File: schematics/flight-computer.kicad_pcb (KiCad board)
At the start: 4 copper layers, 80 x 80 mm, 59 parts, among them J1 BATT, J2 BLACKBOX, J3 BMI-S-201, P1 GPS, P2 TLM, U1 STM32F405RGT6, U2 MAX14787E, U4 MS5611-01BA, U6 Si4463, U7 MAX-M8Q, U8 MAX604, U9 MAX604

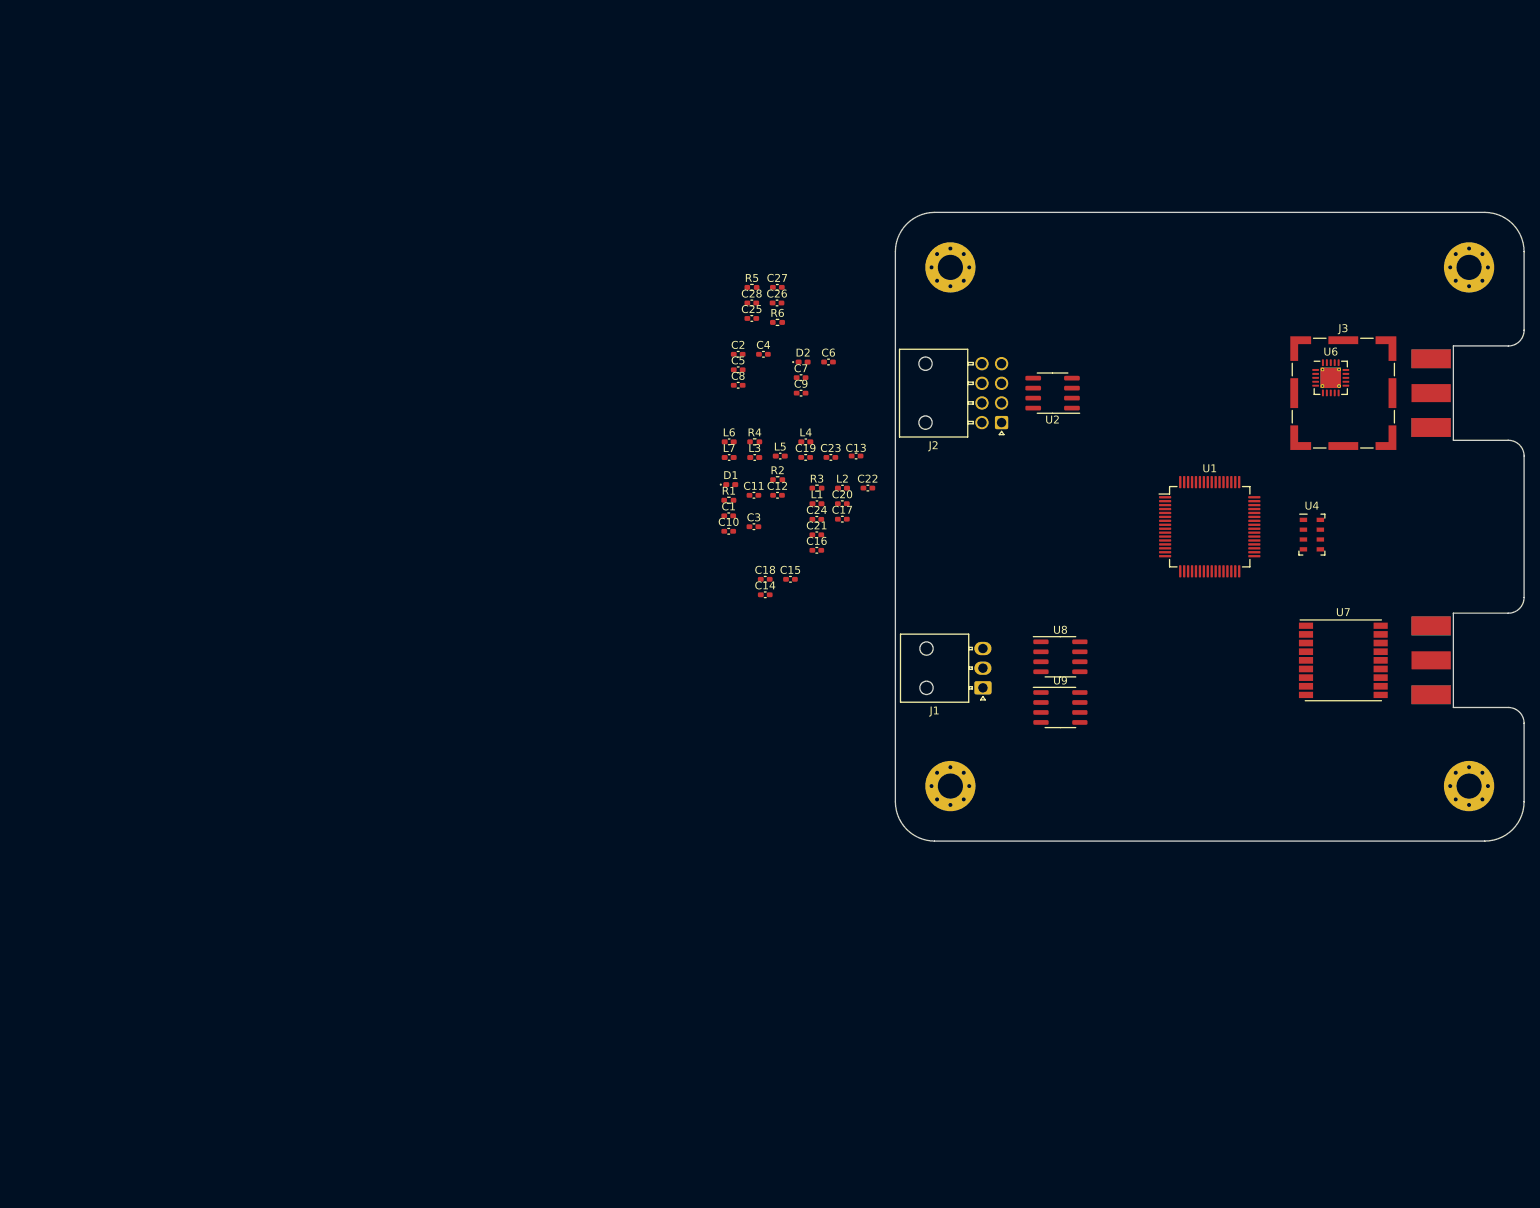
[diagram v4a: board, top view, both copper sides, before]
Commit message: Add missing IC footprints
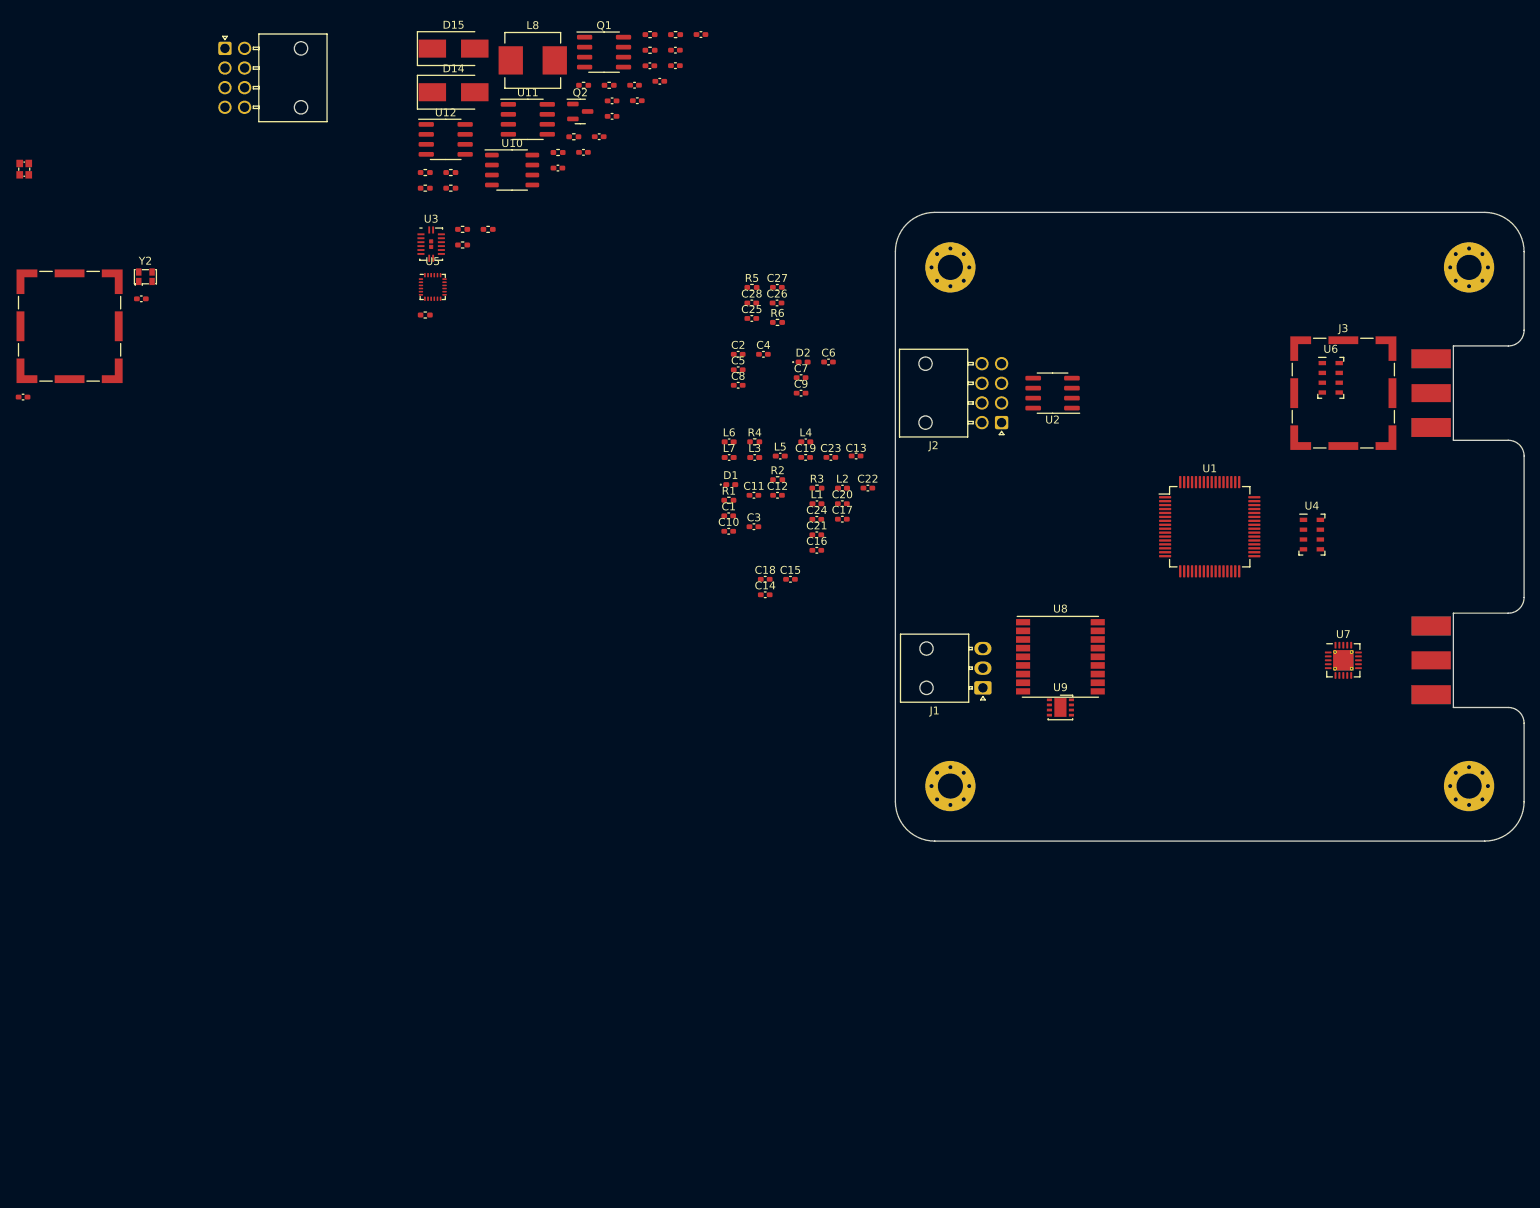
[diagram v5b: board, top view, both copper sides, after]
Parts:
- removed P1: GPS, Strix:SMA-EDGE
- removed P2: TLM, Strix:SMA-EDGE
- added C29: 3p3, Strix:C_0402, F.Cu at (144.0, 118.5)
- added C30: 3p3, Strix:C_0402, F.Cu at (159.1, 106.0)
- added C31: 100n, Strix:C_0402, F.Cu at (218.9, 82.8)
- added C32: 100n, Strix:C_0402, F.Cu at (222.2, 80.8)
- added C33: 330n, Strix:C_0402, F.Cu at (215.3, 87.4)
- added C34: 100n, Strix:C_0402, F.Cu at (221.8, 78.8)
- added C35: 470n, Strix:C_0402, F.Cu at (230.3, 72.4)
- added C36: 10u, Strix:C_0402, F.Cu at (223.8, 76.3)
- added C37: 100n, Strix:C_0402, F.Cu at (227.0, 76.3)
- added C38: 22u, Strix:C_0402, F.Cu at (227.0, 74.4)
- added C39: 10u, Strix:C_0402, F.Cu at (212.1, 89.4)
- added C40: 10u, Strix:C_0402, F.Cu at (218.9, 80.8)
- added C41: 10u, Strix:C_0402, F.Cu at (225.0, 78.3)
- added C42: 10u, Strix:C_0402, F.Cu at (217.3, 85.4)
- added D14: B330, Strix:B330, F.Cu at (198.8, 79.7)
- added D15: B330, Strix:B330, F.Cu at (198.8, 74.2)
- added J4: GPS, Strix:SMA-Edge, F.Cu at (323.2, 152.0)
- added J5: TELEM, Strix:SMA-Edge, F.Cu at (323.2, 118.0)
- added J7: BLACKBOX, Strix:Molex_Nano-Fit_105314-1108, F.Cu at (169.7, 74.1)
- added J8: BMI-S-201, Strix:BMI-S-201, F.Cu at (149.9, 109.5)
- added L8: 6u8, Strix:L_Wuerth_HCI-7050, F.Cu at (208.9, 75.7)
- added Q1: Si9933CDY, Strix:Si9933CDY, F.Cu at (217.9, 74.6)
- added Q2: BSS138, Strix:BSS138, F.Cu at (214.9, 82.2)
- added R10: 4k7, Strix:R_0402, F.Cu at (199.9, 97.2)
- added R11: 100k, Strix:R_0402, F.Cu at (212.1, 87.4)
- added R12: 160, Strix:R_0402, F.Cu at (214.1, 85.4)
- added R13: 261, Strix:R_0402, F.Cu at (223.8, 72.4)
- added R14: 100, Strix:R_0402, F.Cu at (218.6, 78.8)
- added R15: 10k, Strix:R_0402, F.Cu at (215.3, 78.8)
- added R16: 100, Strix:R_0402, F.Cu at (195.2, 89.9)
- added R17: 100, Strix:R_0402, F.Cu at (227.0, 72.4)
- added R18: 2k2, Strix:R_0402, F.Cu at (198.4, 89.9)
- added R19: 50m, Strix:R_0402, F.Cu at (223.8, 74.4)
- added R20: 200k, Strix:R_0402, F.Cu at (195.2, 91.9)
- added R21: 100k, Strix:R_0402, F.Cu at (198.4, 91.9)
- added R7: 4k7, Strix:R_0402, F.Cu at (203.2, 97.2)
- added R8: 200k, Strix:R_0402, F.Cu at (199.9, 99.2)
- added R9: 4k7, Strix:R_0402, F.Cu at (195.2, 108.1)
- added U10: LTC4002-ES8, Strix:LTC4002-ES8, F.Cu at (206.2, 89.6)
- added U11: MAX604, Strix:MAX604, F.Cu at (208.2, 83.2)
- added U12: MAX604, Strix:MAX604, F.Cu at (197.8, 85.7)
- added U3: NVT2006BQ, Strix:NVT2006BQ, F.Cu at (195.9, 99.0)
- added U5: ICM-20789, Strix:ICM-20789, F.Cu at (196.1, 104.5)
- added Y1: 26M, Strix:Xtal-20x16, F.Cu at (144.2, 89.5)
- added Y2: LFTCXO068373, Strix:LFTCXO068373, F.Cu at (159.6, 103.2)
- C1: value 1µ -> 10p
- C10, C11: value 100n -> 2µ2
- C13: value 100n -> 100p
- C14: value 1u -> 15p
- C15: value 2u2 -> 100p
- C16: value 100n -> 15p
- C17: value 220p -> 100n
- C18: value 100p -> 2n
- C19: value 3p -> 100n
- C2: value 4µ7 -> 10p
- C20: value 5p1 -> 1u
- C21: value 1p2 -> 2u2
- C22: value 6n8 -> 100n
- C23: value 3p3 -> 220p
- C24: value 3p3 -> 100p
- C25: value 10u -> 3p
- C26: value 10u -> 5p1
- C27: value 10u -> 1p2
- C28: value 10u -> 6n8
- C3: value 100n -> 1µ
- C4: value 100n -> 4µ7
- C8, C9: value 2µ2 -> 100n
- R1: value 120 -> 100
- R2: value 100k -> 10k
- R4: value 10k -> 120
- R5: value 200k -> 4k7
- R6: value 100k -> 200k
- U6: value Si4463 -> MS5611-01BA; footprint Strix:Si4463 -> Strix:MS5611-01BA
- U7: value MAX-M8Q -> Si4463; footprint Strix:MAX-M8Q -> Strix:Si4463
- U8: value MAX604 -> MAX-M8Q; footprint Strix:MAX604 -> Strix:MAX-M8Q
- U9: value MAX604 -> BQ29200; footprint Strix:MAX604 -> Strix:BQ29200
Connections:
- net /Radio/RADIO_CLK renamed Net-(D5-Pad2)
- C1 pad 2: 3v3 -> Net-(C1-Pad2)
- C10 pad 2: /~{RST} -> Net-(C10-Pad2)
- C11 pad 1: 3v3 -> GND
- C11 pad 2: GND -> Net-(C11-Pad2)
- C12 pad 1: 1v8 -> GND
- C12 pad 2: unconnected-(C12-Pad2) -> /NRST
- C14 pad 1: 3v3 -> GND
- C14 pad 2: GND -> Net-(C14-Pad2)
- C15 pad 1: 3v3 -> GND
- C15 pad 2: GND -> 3v3
- C16 pad 1: 3v3 -> GND
- C16 pad 2: GND -> Net-(C16-Pad2)
- C17 pad 1: 3v3 -> 1v8
- C18 pad 1: 3v3 -> Net-(C18-Pad1)
- C18 pad 2: GND -> Net-(C18-Pad2)
- C19 pad 1: /Radio/RX+ -> GND
- C19 pad 2: GND -> 3v3
- C2 pad 2: 3v3 -> Net-(C2-Pad2)
- C20 pad 1: /Radio/TX -> 3v3
- C20 pad 2: Net-(C20-Pad2) -> GND
- C21 pad 1: /Radio/RX- -> 3v3
- C21 pad 2: Net-(C21-Pad2) -> GND
- C22 pad 1: Net-(C21-Pad2) -> 3v3
- C23 pad 1: Net-(C23-Pad1) -> 3v3
- C24 pad 1: Net-(C24-Pad1) -> 3v3
- C25 pad 1: VBATT -> /Radio/RX+
- C26 pad 1: VBATT -> /Radio/TX
- C26 pad 2: GND -> Net-(C26-Pad2)
- C27 pad 1: 3v3 -> /Radio/RX-
- C27 pad 2: GND -> Net-(C27-Pad2)
- C28 pad 1: 1v8 -> Net-(C27-Pad2)
- C8 pad 2: Net-(C8-Pad2) -> 3v3
- C9 pad 2: Net-(C9-Pad2) -> 3v3
- J1 pad 1: /PSU/BATT+ -> VBATT
- J1 pad 3: /PSU/BATT- -> GND
- L3 pad 1: Net-(C20-Pad2) -> Net-(C26-Pad2)
- L3 pad 2: Net-(C21-Pad2) -> Net-(C27-Pad2)
- L4 pad 2: Net-(C21-Pad2) -> Net-(C27-Pad2)
- L5 pad 1: Net-(C21-Pad2) -> Net-(C27-Pad2)
- L5 pad 2: Net-(C23-Pad1) -> Net-(C29-Pad1)
- L6 pad 1: Net-(C23-Pad1) -> Net-(C29-Pad1)
- L6 pad 2: Net-(C24-Pad1) -> Net-(C30-Pad1)
- L7 pad 1: Net-(C24-Pad1) -> Net-(C30-Pad1)
- R1 pad 1: /UART4_RX+ -> Net-(C2-Pad2)
- R1 pad 2: /UART4_RX- -> Net-(R1-Pad2)
- R2 pad 1: 1v8 -> GND
- R2 pad 2: GND -> /USB_FS_VBUS
- R3 pad 1: /Radio/RADIO_CLK_1.65V -> /USB_FS_VBUS
- R4 pad 1: /Radio/RADIO_CLK_1.65V -> /BB_RX+
- R4 pad 2: GND -> /BB_RX-
- R5 pad 1: Net-(R5-Pad1) -> 3v3
- R5 pad 2: GND -> /IMU_PR_CL
- R6 pad 1: Net-(R5-Pad1) -> 3v3
- R6 pad 2: 1v8 -> Net-(C14-Pad2)
- U1 pad 31: Net-(C8-Pad2) -> Net-(C10-Pad2)
- U1 pad 42: unconnected-(U1-Pad42) -> /USB_FS_VBUS
- U1 pad 44: unconnected-(U1-Pad44) -> /USB_FS_D+
- U1 pad 45: unconnected-(U1-Pad45) -> /USB_FS_D-
- U1 pad 47: Net-(C9-Pad2) -> Net-(C11-Pad2)
- U1 pad 5: /MCU_CLK -> Net-(C1-Pad2)
- U1 pad 50: unconnected-(U1-Pad50) -> /CHG_SDN
- U1 pad 58: unconnected-(U1-Pad58) -> /IMU_PR_CL
- U1 pad 59: unconnected-(U1-Pad59) -> /IMU_PR_DA
- U1 pad 6: unconnected-(U1-Pad6) -> Net-(R1-Pad2)
- U1 pad 7: /~{RST} -> /NRST
- U2 pad 5: /UART4_TX+ -> /BB_TX+
- U2 pad 6: /UART4_TX- -> /BB_TX-
- U2 pad 7: /UART4_RX- -> /BB_RX-
- U2 pad 8: /UART4_RX+ -> /BB_RX+
- U6 pad 1: /RADIO_SDN -> 3v3
- U6 pad 2: /Radio/RX+ -> GND
- U6 pad 3: /Radio/RX- -> GND
- U6 pad 4: /Radio/TX -> /BARO_~{CS}
- U6 pad 5: unconnected-(U6-Pad5) -> /BARO_~{CS}
- U6 pad 6: 3v3 -> /SPI3_MISO
- U6 pad 7: unconnected-(U6-Pad7) -> /SPI3_MOSI
- U6 pad 8: 3v3 -> /SPI3_SCLK
- U7 pad 1: GND -> /RADIO_SDN
- U7 pad 10: GND -> unconnected-(U7-Pad10)
- U7 pad 11: /Radio/ANT_GPS -> /RADIO_~{INT}
- U7 pad 12: GND -> /SPI2_SCLK
- U7 pad 13: unconnected-(U7-Pad13) -> /SPI2_MISO
- U7 pad 14: unconnected-(U7-Pad14) -> /SPI2_MOSI
- U7 pad 15: unconnected-(U7-Pad15) -> /RADIO_~{CS}
- U7 pad 17: unconnected-(U7-Pad17) -> Net-(C18-Pad2)
- U7 pad 18: unconnected-(U7-Pad18) -> GND
- U7 pad 2: /USART3_RX -> /Radio/RX+
- U7 pad 3: /USART3_TX -> /Radio/RX-
- U7 pad 4: unconnected-(U7-Pad4) -> /Radio/TX
- U7 pad 7: 3v3 -> unconnected-(U7-Pad7)
- U7 pad 9: /GPS_~{RESET} -> unconnected-(U7-Pad9)
- U8 pad 1: VBATT -> GND
- U8 pad 2: GND -> /USART3_RX
- U8 pad 3: GND -> /USART3_TX
- U8 pad 4: VBATT -> unconnected-(U8-Pad4)
- U8 pad 5: GND -> unconnected-(U8-Pad5)
- U8 pad 6: GND -> 3v3
- U8 pad 7: GND -> 3v3
- U9 pad 1: VBATT -> Net-(C31-Pad1)
- U9 pad 2: GND -> Net-(C31-Pad2)
- U9 pad 3: GND -> Net-(R14-Pad2)
- U9 pad 4: VBATT -> Net-(C33-Pad1)
- U9 pad 5: Net-(R5-Pad1) -> GND
- U9 pad 7: GND -> Net-(C37-Pad1)
- U9 pad 8: 1v8 -> unconnected-(U9-Pad8)

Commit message: Fix outdated footprint references in symbol lib
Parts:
- removed J2: BLACKBOX, Strix:Molex_Nano-Fit_105314-1108
- removed J3: BMI-S-201, Strix:BMI-S-201
- added D10: D_ESD, Strix:D_0402, F.Cu at (167.6, 121.0)
- added D11: D_ESD, Strix:D_0402, F.Cu at (154.0, 123.6)
- added D12: D_ESD, Strix:D_0402, F.Cu at (168.0, 123.0)
- added D13: D_ESD, Strix:D_0402, F.Cu at (187.8, 100.1)
- added D3: D_ESD, Strix:D_0402, F.Cu at (164.5, 123.6)
- added D4: D_ESD, Strix:D_0402, F.Cu at (161.0, 123.6)
- added D5: D_ESD, Strix:D_0402, F.Cu at (187.8, 104.1)
- added D6: D_ESD, Strix:D_0402, F.Cu at (176.0, 114.6)
- added D7: D_ESD, Strix:D_0402, F.Cu at (157.5, 123.6)
- added D8: D_ESD, Strix:D_0402, F.Cu at (187.8, 102.1)
- added D9: D_ESD, Strix:D_0402, F.Cu at (184.3, 106.0)
- D1, D2: value ESD_DIODE -> D_ESD
- U4: value MS5611-01BA -> PCA9306; footprint Strix:MS5611-01BA -> Strix:PCA9306
- moved U1 123.2 mm to (175.2, 106.4)
- moved U9 121.6 mm to (154.8, 147.7)
- moved J1 119.0 mm to (154.3, 114.9), turned to 0 degrees
- moved U6 115.4 mm to (197.0, 137.6)
- moved U4 109.2 mm to (198.9, 131.1)
- moved U2 105.1 mm to (169.9, 116.8), turned to 0 degrees
- moved U7 100.5 mm to (219.0, 113.9)
- moved R13 90.6 mm to (170.7, 145.8)
- moved R19 84.6 mm to (172.7, 141.8)
- moved C37 83.9 mm to (177.1, 143.8)
- moved C40 82.6 mm to (170.7, 147.8)
- moved R17 82.3 mm to (173.9, 135.3)
- moved C32 80.9 mm to (173.9, 145.8)
- moved C34 80.7 mm to (173.9, 143.8)
- moved C35 77.9 mm to (183.7, 134.8)
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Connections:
- D1 pad 1: /Radio/ANT_GPS -> /PSU/BATT_MON
- D2 pad 1: /Radio/ANT_TLM -> /PSU/CHG+
- U4 pad 1: 3v3 -> GND
- U4 pad 2: GND -> 1v8
- U4 pad 3: GND -> Net-(R9-Pad2)
- U4 pad 4: /BARO_~{CS} -> Net-(R10-Pad2)
- U4 pad 5: /BARO_~{CS} -> /IMU_PR_DA
- U4 pad 6: /SPI3_MISO -> /IMU_PR_CL
- U4 pad 7: /SPI3_MOSI -> 3v3
- U4 pad 8: /SPI3_SCLK -> Net-(C16-Pad2)

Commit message: Preliminary board layout
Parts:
- added D16: B330, Strix:B330, F.Cu at (216.8, 214.2)
- added J2: CHG, Strix:Molex_Nano-Fit_105313-1102, F.Cu at (288.2, 164.1)
- added J3: SWD, Strix:Header_SWD, F.Cu at (289.1, 100.7)
- added J6: GPS, Strix:SMA-Edge, F.Cu at (323.2, 152.0)
- added J9: Expansion Slot, Strix:Header_RaspberryPi, F.Cu at (260.7, 110.9)
- D14: value B330 -> D_ESD; footprint Strix:B330 -> Strix:D_0402
- J4: value GPS -> BLACKBOX; footprint Strix:SMA-Edge -> Strix:Molex_Nano-Fit_105314-1108
- J5: value TELEM -> USB C; footprint Strix:SMA-Edge -> Strix:USB_C
- J7: value BLACKBOX -> TELEM; footprint Strix:Molex_Nano-Fit_105314-1108 -> Strix:SMA-Edge
- R1: value 100 -> 120
- R2: value 10k -> 100
- R4: value 120 -> 10k
- U1: value STM32F405RGT6 -> MAX14787E; footprint Strix:STM32F405RGT6 -> Strix:MAX14787E
- U2: value MAX14787E -> STM32F405RGT6; footprint Strix:MAX14787E -> Strix:STM32F405RGT6
- U3: value NVT2006BQ -> SOT763-1 (DHVQFN16)
- moved J7 169.9 mm to (323.2, 118.0), turned to -90 degrees
- moved D7 164.7 mm to (321.2, 105.9)
- moved D14 163.1 mm to (319.7, 120.5), turned to -90 degrees
- moved D4 161.5 mm to (321.2, 103.7)
- moved D11 155.5 mm to (304.5, 162.8), turned to 180 degrees
- moved U9 147.2 mm to (297.5, 183.8)
- moved D6 145.6 mm to (321.2, 104.9)
- moved D13 142.8 mm to (319.8, 154.8), turned to -90 degrees
- moved D10 142.6 mm to (304.5, 160.8), turned to 180 degrees
- moved R3 142.0 mm to (312.0, 165.0)
- moved D12 141.9 mm to (304.5, 161.8), turned to 180 degrees
- moved R4 139.7 mm to (312.0, 164.0), turned to 180 degrees
- moved D9 137.0 mm to (321.2, 108.9)
- moved R17 135.9 mm to (301.4, 182.4)
- moved J1 134.3 mm to (279.2, 164.1), turned to -90 degrees
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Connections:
- D10 pad 2: /BB_TX- -> Net-(D10-Pad2)
- D11 pad 1: /Radio/ANT_GPS -> GND
- D11 pad 2: GND -> /USB_FS_D-
- D12 pad 1: /Radio/ANT_TLM -> GND
- D12 pad 2: GND -> /USB_FS_D+
- D13 pad 1: GND -> /Radio/ANT_GPS
- D13 pad 2: /BB_TX- -> GND
- D14 pad 1: Net-(C34-Pad1) -> /Radio/ANT_TLM
- D14 pad 2: /PSU/CHG+ -> GND
- D15 pad 1: Net-(D15-Pad1) -> Net-(C34-Pad1)
- D15 pad 2: GND -> /PSU/CHG+
- D4 pad 2: 3v3 -> /BB_TX+
- D5 pad 2: Net-(D5-Pad2) -> /BB_RX+
- D6 pad 2: /BB_RX- -> 3v3
- D7 pad 2: /USB_FS_D- -> 3v3
- D8 pad 2: /BB_TX+ -> /BB_RX-
- D9 pad 2: /USB_FS_D+ -> /BB_TX-
- J4 pad 1: /Radio/ANT_GPS -> 3v3
- J4 pad 2: GND -> 3v3
- J7 pad 1: 3v3 -> /Radio/ANT_TLM
- J7 pad 2: 3v3 -> GND
- L8 pad 1: Net-(D15-Pad1) -> Net-(D16-Pad1)
- Q1 pad 7: Net-(D15-Pad1) -> Net-(D16-Pad1)
- Q1 pad 8: Net-(D15-Pad1) -> Net-(D16-Pad1)
- R1 pad 1: Net-(C2-Pad2) -> /BB_RX+
- R1 pad 2: Net-(R1-Pad2) -> /BB_RX-
- R2 pad 1: GND -> Net-(C2-Pad2)
- R2 pad 2: /USB_FS_VBUS -> Net-(R2-Pad2)
- R3 pad 1: /USB_FS_VBUS -> GND
- R3 pad 2: Net-(D5-Pad2) -> /USB_FS_VBUS
- R4 pad 1: /BB_RX+ -> /USB_FS_VBUS
- R4 pad 2: /BB_RX- -> Net-(D10-Pad2)
- U1 pad 2: /BARO_~{CS} -> /UART4_RX
- U1 pad 3: unconnected-(U1-Pad3) -> /UART4_TX
- U1 pad 4: unconnected-(U1-Pad4) -> GND
- U1 pad 5: Net-(C1-Pad2) -> /BB_TX+
- U1 pad 6: Net-(R1-Pad2) -> /BB_TX-
- U1 pad 7: /NRST -> /BB_RX-
- U1 pad 8: unconnected-(U1-Pad8) -> /BB_RX+
- U2 pad 2: /UART4_RX -> /BARO_~{CS}
- U2 pad 3: /UART4_TX -> unconnected-(U2-Pad3)
- U2 pad 4: GND -> unconnected-(U2-Pad4)
- U2 pad 5: /BB_TX+ -> Net-(C1-Pad2)
- U2 pad 6: /BB_TX- -> Net-(R2-Pad2)
- U2 pad 7: /BB_RX- -> /NRST
- U2 pad 8: /BB_RX+ -> unconnected-(U2-Pad8)
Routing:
- net GND: vias 0 -> 15
- added copper zone on B.Cu, net GND
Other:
- board text added: "2022 CU Spaceflight"
- board text added: "LYCHEE"

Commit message: Rough power and RF layouts
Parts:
- U3: value SOT763-1 (DHVQFN16) -> NVT2006BQ
- moved R16 116.6 mm to (290.9, 153.7), turned to -90 degrees
- moved R15 114.4 mm to (289.1, 154.2), turned to 180 degrees
- moved Q2 109.5 mm to (290.1, 156.7)
- moved C35 109.2 mm to (291.8, 158.9), turned to 180 degrees
- moved R18 107.4 mm to (289.4, 158.9)
- moved C40 94.4 mm to (292.2, 147.4), turned to -90 degrees
- moved R21 93.7 mm to (301.9, 150.0)
- moved U12 93.4 mm to (296.5, 148.7)
- moved D15 93.4 mm to (282.1, 167.0), turned to -90 degrees
- moved R20 92.8 mm to (300.8, 150.0), turned to 90 degrees
- moved C42 92.5 mm to (300.8, 147.4)
- moved C39 84.2 mm to (287.6, 146.5), turned to 0 degrees
- moved D16 84.2 mm to (274.9, 153.3), turned to 0 degrees
- moved U11 82.9 mm to (288.8, 142.2), turned to 90 degrees
- moved R11 81.8 mm to (272.9, 157.9), turned to 180 degrees
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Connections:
- net Net-(C34-Pad1) renamed /PSU/VCC_CHG
- net Net-(C35-Pad1) renamed /PSU/COMP
- net Net-(D16-Pad1) renamed /PSU/V_SW
- net Net-(L8-Pad2) renamed /PSU/SENSE
- net Net-(Q1-Pad4) renamed /PSU/~{CHRG}
- D4 pad 2: /BB_TX+ -> /BB_TX-
- D5 pad 2: /BB_RX+ -> /BB_RX-
- D8 pad 2: /BB_RX- -> /BB_RX+
- D9 pad 2: /BB_TX- -> /BB_TX+
- J4 pad 3: /BB_RX+ -> /BB_RX-
- J4 pad 4: /BB_RX- -> /BB_RX+
- J4 pad 5: /BB_TX+ -> /BB_TX-
- J4 pad 6: /BB_TX- -> /BB_TX+
- J9 pad 1: unconnected-(J9-Pad1) -> 3v3
- J9 pad 10: unconnected-(J9-Pad10) -> /EXT_RX
- J9 pad 14: unconnected-(J9-Pad14) -> GND
- J9 pad 17: unconnected-(J9-Pad17) -> 3v3
- J9 pad 19: unconnected-(J9-Pad19) -> /EXT_MOSI
- J9 pad 20: unconnected-(J9-Pad20) -> GND
- J9 pad 21: unconnected-(J9-Pad21) -> /EXT_MISO
- J9 pad 23: unconnected-(J9-Pad23) -> /EXT_SCLK
- J9 pad 25: unconnected-(J9-Pad25) -> GND
- J9 pad 3: unconnected-(J9-Pad3) -> /EXT_SDA
- J9 pad 30: unconnected-(J9-Pad30) -> GND
- J9 pad 34: unconnected-(J9-Pad34) -> GND
- J9 pad 39: unconnected-(J9-Pad39) -> GND
- J9 pad 5: unconnected-(J9-Pad5) -> /EXT_SCL
- J9 pad 6: unconnected-(J9-Pad6) -> GND
- J9 pad 8: unconnected-(J9-Pad8) -> /EXT_TX
- J9 pad 9: unconnected-(J9-Pad9) -> GND
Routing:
- net GND: track 0.00 -> 48.7 mm, vias 15 -> 24
- net 1v8: track 0.00 -> 24.5 mm, vias 0 -> 2
- net /BB_TX-: track 0.00 -> 21.9 mm
- net /PSU/~{CHRG}: track 0.00 -> 20.3 mm, vias 0 -> 3
- net /BB_TX+: track 0.00 -> 19.6 mm
- net 3v3: track 0.00 -> 18.7 mm
- net /PSU/BATT_MON: track 0.00 -> 17.7 mm, vias 0 -> 1
- net /NRST: track 0.00 -> 17.0 mm
- net /Radio/ANT_TLM: track 0.00 -> 13.6 mm
- net Net-(Q1-Pad2): track 0.00 -> 13.0 mm
- net /SWO: track 0.00 -> 12.8 mm
- net /Radio/ANT_GPS: track 0.00 -> 11.9 mm
- net /BB_RX-: track 0.00 -> 11.9 mm
- net /SWCLK: track 0.00 -> 11.8 mm
- net /BB_RX+: track 0.00 -> 11.3 mm
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- added copper zone on F.Cu, net /CHG_SDN
- added copper zone on F.Cu, net /PSU/CHG+
- added copper zone on F.Cu, net /PSU/COMP
- added copper zone on F.Cu, net /PSU/SENSE
- added copper zone on F.Cu, net /PSU/VCC_CHG
- added copper zone on F.Cu, net /PSU/V_SW
- added copper zone on F.Cu, net 1v8
- added copper zone on F.Cu, net 3v3
- added copper zone on In2.Cu, net 3v3
- added copper zone on F.Cu, net GND
- added copper zone on In1.Cu, net GND
- added copper zone on F.Cu, net VBATT
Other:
- rule pad_to_mask_clearance: 0 -> 0.05
